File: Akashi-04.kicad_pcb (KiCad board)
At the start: 2 copper layers, 71.1 x 67.3 mm, 14 parts, among them CN10 PPPC192LFBN-RC, CN7 PPPC192LFBN-RC

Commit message: Designe done
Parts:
- removed D3, D4: LED, LED_THT:LED_D3.0mm_Clear
- removed R4: 1k, Resistor_THT:R_Axial_DIN0207_L6.3mm_D2.5mm_P10.16mm_Horizontal
- removed TP11, TP12: GND, TestPoint:TestPoint_THTPad_D2.0mm_Drill1.0mm
- added CN5: Conn_01x10, Connector_PinHeader_2.54mm:PinHeader_1x10_P2.54mm_Vertical, F.Cu at (175.3, 85.1)
- added CN6: Conn_01x08, Connector_PinHeader_2.54mm:PinHeader_1x08_P2.54mm_Vertical, F.Cu at (127.0, 71.1)
- added CN8: Conn_01x06, Connector_PinHeader_2.54mm:PinHeader_1x06_P2.54mm_Vertical, F.Cu at (127.0, 94.0)
- added CN9: Conn_01x08, Connector_PinHeader_2.54mm:PinHeader_1x08_P2.54mm_Vertical, F.Cu at (175.3, 106.7)
- added JP1: SolderJumper_2_Bridged, Jumper:SolderJumper-2_P1.3mm_Bridged_RoundedPad1.0x1.5mm, B.Cu at (154.9, 71.1)
- added JP2: SolderJumper_2_Bridged, Jumper:SolderJumper-2_P1.3mm_Bridged_RoundedPad1.0x1.5mm, B.Cu at (154.9, 62.9)
- added JP3: SolderJumper_2_Open, Jumper:SolderJumper-2_P1.3mm_Open_RoundedPad1.0x1.5mm, B.Cu at (147.9, 68.6)
- added JP4: SolderJumper_2_Open, Jumper:SolderJumper-2_P1.3mm_Open_RoundedPad1.0x1.5mm, B.Cu at (148.0, 61.0)
- added U1: UMB-ADAU1361A, Codec_Modules:UMB-ADAU1361A, F.Cu at (162.6, 91.4)
- R3: value 1k -> 4.7k
- moved R9 47.6 mm to (175.3, 41.9), turned to 270 degrees
- moved R5 42.7 mm to (180.3, 41.9), turned to 270 degrees
- moved R3 25.7 mm to (133.3, 81.3)
- moved D1 22.5 mm to (135.9, 106.7), turned to 180 degrees
- moved R1 21.0 mm to (133.3, 97.8), turned to 0 degrees
- moved D2 15.2 mm to (144.8, 106.7), turned to 180 degrees
- moved R2 12.5 mm to (133.3, 101.6), turned to 0 degrees
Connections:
- CN7 pad 1: /I2S3_CK -> /I2S2_CK
- CN7 pad 17: /I2S3_WS -> /I2S2_WS
- CN7 pad 36: /LED4 -> Net-(CN7-Pad36)
- CN7 pad 38: /LED3 -> Net-(CN7-Pad38)
- R3 pad 1: /LED3 -> +3V3
- R5 pad 2: /I2C1_SCL -> Net-(R5-Pad2)
- R9 pad 2: /I2C1_SDA -> Net-(R9-Pad2)
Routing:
- net +3V3: track 0.00 -> 103.3 mm
- net /I2S2_CK: track 0.00 -> 85.1 mm
- net /I2S2_WS: track 0.00 -> 71.3 mm
- net /I2S3_SD: track 0.00 -> 50.8 mm
- net /I2S2_SD: track 0.00 -> 25.8 mm
- net Net-(R5-Pad2): track 0.00 -> 23.6 mm
- net Net-(JP3-Pad2): track 0.00 -> 22.6 mm
- net Net-(R9-Pad2): track 0.00 -> 17.4 mm
- net /LED1: track 0.00 -> 16.8 mm
- net /LED2: track 0.00 -> 16.3 mm
- net Net-(JP1-Pad1): track 0.00 -> 15.5 mm
- net Net-(JP2-Pad1): track 0.00 -> 15.0 mm
- net Net-(D1-Pad2): track 0.00 -> 13.8 mm
- net GND: track 0.00 -> 5.86 mm, vias 0 -> 2
- net /I2C1_SDA: track 0.00 -> 5.61 mm
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- added copper zone on F.Cu, net GND
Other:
- board size 71.1 x 67.3 mm -> 71.1 x 74.9 mm
- net class +3V3 added: clearance 0.2, trace_width 0.5, via_dia 0.8, via_drill 0.4
- board text added: "(C) Seiichi Horie 2020 https://github.com/suikan4github/Akashi-04"
- board text added: "Address 0x38 – Default 0x39 0x3A 0x3B"
- board text added: "Akashi-04 v1.0.0 For Nucleo-G431RB"
- board text added: "CODEC I2C Address"
- board text added: "JP1 Closed Open Closed Open"
- board text added: "JP2 Closed Closed Open Open"
- board text added: "JP3 Open Closed Open Closed"
- board text added: "JP4 Open Open Closed Closed"
- board text added: "UMB-ADAU1361-A"
- board text removed: "Akashi-04 v1.0.0 Audio for Nucleo-G431RB (C) Seiichi Horie 2019 https://github.com/suikan4github/Akashi-04"

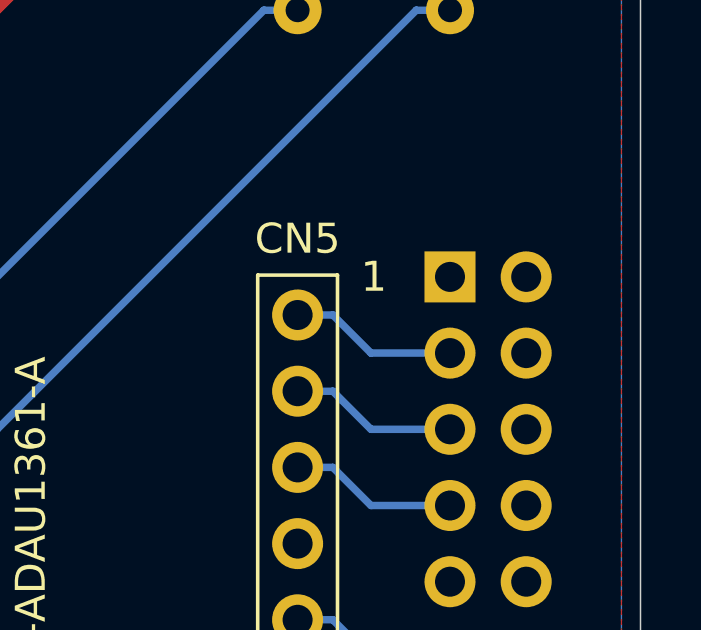
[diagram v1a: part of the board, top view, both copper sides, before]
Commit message: Added I2C clock rescue
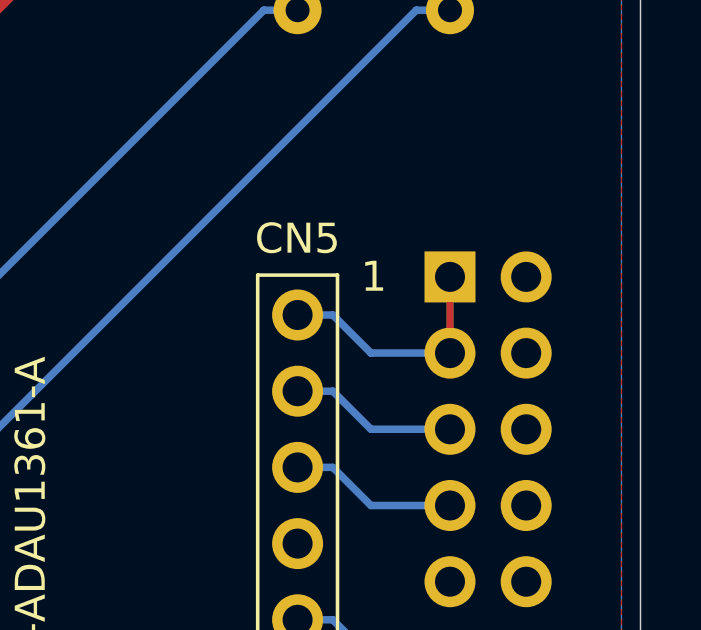
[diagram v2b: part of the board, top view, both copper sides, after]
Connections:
- CN10 pad 1: Net-(CN10-Pad1) -> /I2C1_SCL
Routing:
- net /I2C1_SCL: track 5.61 -> 8.15 mm

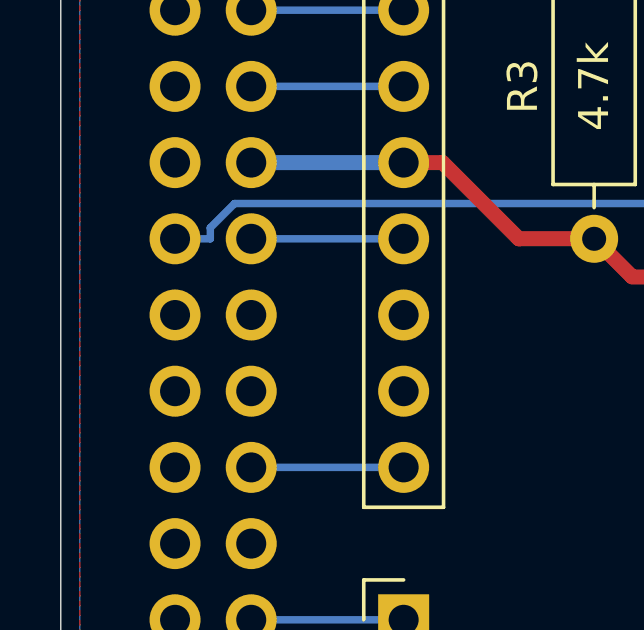
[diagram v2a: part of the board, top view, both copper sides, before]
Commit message: Added rescue line of I2C and I2S WS int
I2C rescue is needed to toggle the I2C SCL inc case of
the device is stretching signal by fault.

I2S WS int is needed to start the audio in the correct timing.
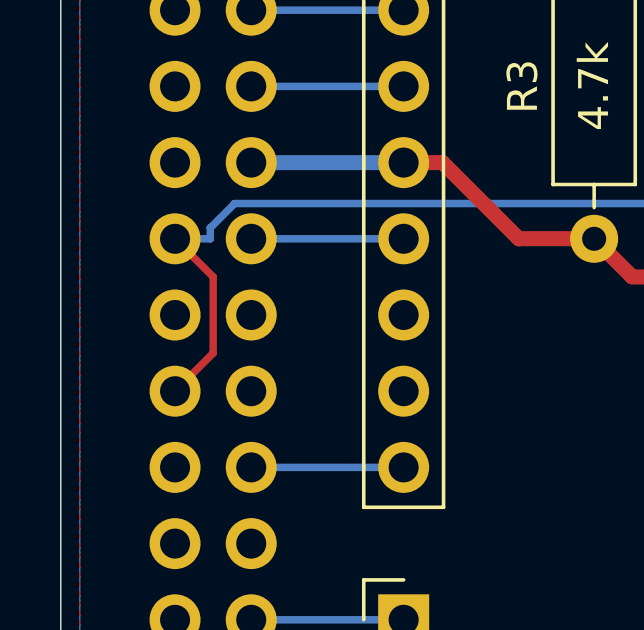
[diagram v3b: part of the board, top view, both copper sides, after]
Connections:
- CN7 pad 21: Net-(CN7-Pad21) -> /I2S2_WS
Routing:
- net /I2S2_WS: track 71.3 -> 77.4 mm

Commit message: Generated v1.0.0 gerber
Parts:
- moved JP3 2.54 mm to (147.9, 71.1)
- moved JP4 2.54 mm to (148.0, 63.5)
- moved JP2 0.90 mm to (155.6, 63.5), turned to 180 degrees
- moved JP1 0.65 mm to (155.6, 71.1), turned to 180 degrees
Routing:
- net GND: track 5.86 -> 0.00 mm, vias 2 -> 0
- net Net-(JP2-Pad1): track 15.0 -> 17.6 mm, vias 0 -> 1
- net Net-(JP1-Pad1): track 15.5 -> 17.5 mm
- added copper zone on F.Cu, net Net-(CN10-Pad38)
- removed copper zone on F.Cu, net GND
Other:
- board size 71.1 x 74.9 mm -> 69.9 x 74.9 mm

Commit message: Update v1.0.1
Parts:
- removed JP3, JP4: SolderJumper_2_Open, Jumper:SolderJumper-2_P1.3mm_Open_RoundedPad1.0x1.5mm
- added R4: 4.7k, Resistor_THT:R_Axial_DIN0207_L6.3mm_D2.5mm_P10.16mm_Horizontal, B.Cu at (146.1, 85.1)
- R3: moved to B.Cu
- moved R3 18.2 mm to (151.1, 85.1)
- moved JP1 2.54 mm to (155.6, 68.6)
- moved JP2 2.54 mm to (155.6, 61.0)
- renumbered R9 to R6
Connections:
- R3 pad 2: Net-(JP3-Pad2) -> Net-(JP1-Pad1)
- R5 pad 2: Net-(R5-Pad2) -> /I2C1_SDA
- R6 pad 2: Net-(R9-Pad2) -> /I2C1_SCL
- U1 pad 11: Net-(R5-Pad2) -> /I2C1_SDA
- U1 pad 12: Net-(R9-Pad2) -> /I2C1_SCL
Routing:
- net /I2C1_SDA: track 5.61 -> 32.6 mm
- net Net-(R5-Pad2): track 23.6 -> 0.00 mm
- net /I2C1_SCL: track 8.15 -> 31.0 mm
- net Net-(JP3-Pad2): track 22.7 -> 0.00 mm
- net Net-(R9-Pad2): track 17.4 -> 0.00 mm
- net /I2S2_WS: track 77.4 -> 84.4 mm
- net Net-(JP2-Pad1): track 17.6 -> 24.5 mm, vias 1 -> 0
- net Net-(JP1-Pad1): track 17.5 -> 15.4 mm
- net /I2S2_CK: track 85.1 -> 83.6 mm
- net GND: vias 0 -> 1
- added copper zone on F.Cu, net GND
- removed copper zone on F.Cu, net Net-(CN10-Pad38)
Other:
- board text added: "Akashi-04 v1.0.1 For Nucleo-G431RB"
- board text added: "R3 and R4 must be installed only when JP1 and JP2 is cut, respectively"
- board text removed: "Akashi-04 v1.0.0 For Nucleo-G431RB"
- board text removed: "JP3 Open Closed Open Closed"
- board text removed: "JP4 Open Open Closed Closed"

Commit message: Moved resister
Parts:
- R3, R4: moved to F.Cu
- moved R4 41.2 mm to (168.9, 50.8), turned to 270 degrees
- moved R3 18.9 mm to (168.9, 78.7)
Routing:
- net Net-(JP2-Pad1): track 24.5 -> 12.7 mm
- net /I2S2_WS: track 84.4 -> 77.1 mm
- net +3V3: track 103.2 -> 106.8 mm
- net Net-(JP1-Pad1): track 15.4 -> 12.7 mm
- net /I2S2_CK: track 83.6 -> 84.7 mm
- net GND: vias 1 -> 3
